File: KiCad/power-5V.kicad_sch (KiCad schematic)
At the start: 0 parts

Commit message: chore(pcb): split voltage regulators to separate schematics
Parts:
- added U?: TPS84320RUQR, RUQ_47, symbol Buck converter:TPS84320RUQR
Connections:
- new net 5V: U?.21 (VO), U?.24 (VO), U?.25 (VO), U?.26 (VO), U?.27 (VO), U?.28 (VO), U?.29 (VO), U?.47 (VO)
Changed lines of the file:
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@@
 (kicad_sch (version 20211123) (generator eeschema)
   (paper "A4")
+  (junction (at 178.6128 78.3336) (diameter 0) (color 0 0 0 0)
+  )
+  (junction (at 178.6128 80.8736) (diameter 0) (color 0 0 0 0)
+  )
+  (junction (at 178.6128 75.7936) (diameter 0) (color 0 0 0 0)
+  )
+  (junction (at 178.6128 73.2536) (diameter 0) (color 0 0 0 0)
+  )
+  (junction (at 178.6128 68.1736) (diameter 0) (color 0 0 0 0)
+  )
+  (junction (at 178.6128 70.7136) (diameter 0) (color 0 0 0 0)
+  )
+  (junction (at 178.6128 65.6336) (diameter 0) (color 0 0 0 0)
+  )
+  (wire (pts (xy 178.6128 80.8736) (xy 178.6128 83.4136))
+    (stroke (width 0) (type default) (color 0 0 0 0))
+  )
+  (wire (pts (xy 178.6128 70.7136) (xy 178.6128 73.2536))
+    (stroke (width 0) (type default) (color 0 0 0 0))
+  )
+  (wire (pts (xy 178.6128 75.7936) (xy 178.6128 78.3336))
+    (stroke (width 0) (type default) (color 0 0 0 0))
+  )
+  (wire (pts (xy 178.6128 63.0936) (xy 181.1528 63.0936))
+    (stroke (width 0) (type default) (color 0 0 0 0))
+  )
+  (wire (pts (xy 178.6128 78.3336) (xy 178.6128 80.8736))
+    (stroke (width 0) (type default) (color 0 0 0 0))
+  )
+  (wire (pts (xy 178.6128 65.6336) (xy 178.6128 68.1736))
+    (stroke (width 0) (type default) (color 0 0 0 0))
+  )
+  (wire (pts (xy 178.6128 63.0936) (xy 178.6128 65.6336))
+    (stroke (width 0) (type default) (color 0 0 0 0))
+  )
+  (wire (pts (xy 178.6128 73.2536) (xy 178.6128 75.7936))
+    (stroke (width 0) (type default) (color 0 0 0 0))
+  )
+  (wire (pts (xy 178.6128 68.1736) (xy 178.6128 70.7136))
+    (stroke (width 0) (type default) (color 0 0 0 0))
+  )
+  (global_label "5V" (shape input) (at 181.1528 63.0936 0) (fields_autoplaced)
+    (effects (font (size 1.27 1.27)) (justify left))
+    (property "Intersheet References" "${INTERSHEET_REFS}" (id 0) (at 185.864 63.0142 0)
+      (effects (font (size 1.27 1.27)) (justify left) hide)
+    )
+  )
+  (symbol (lib_id "Buck converter:TPS84320RUQR") (at 127.8128 55.4736 0) (unit 1)
+    (in_bom yes) (on_board yes) (fields_autoplaced)
+    (property "Reference" "U?" (id 0) (at 153.2128 44.0436 0)
+      (effects (font (size 1.524 1.524)))
+    )
+    (property "Value" "TPS84320RUQR" (id 1) (at 153.2128 47.8536 0)
+      (effects (font (size 1.524 1.524)))
+    )
+    (property "Footprint" "RUQ_47" (id 2) (at 153.2128 49.3776 0)
+      (effects (font (size 1.524 1.524)) hide)
+    )
+    (property "Datasheet" "" (id 3) (at 127.8128 55.4736 0)
+      (effects (font (size 1.524 1.524)))
+    )
+    (pin "1")
+    (pin "10")
+    (pin "11")
+    (pin "12")
+    (pin "13")
+    (pin "14")
+    (pin "15")
+    (pin "16")
+    (pin "17")
+    (pin "18")
+    (pin "19")
+    (pin "2")
+    (pin "20")
+    (pin "21")
+    (pin "22")
+    (pin "23")
+    (pin "24")
+    (pin "25")
+    (pin "26")
+    (pin "27")
+    (pin "28")
+    (pin "29")
+    (pin "3")
+    (pin "30")
+    (pin "31")
+    (pin "32")
+    (pin "33")
+    (pin "34")
+    (pin "35")
+    (pin "36")
+    (pin "37")
+    (pin "38")
+    (pin "39")
+    (pin "4")
+    (pin "40")
+    (pin "41")
+    (pin "42")
+    (pin "43")
+    (pin "44")
+    (pin "45")
+    (pin "46")
+    (pin "47")
+    (pin "5")
+    (pin "6")
+    (pin "7")
+    (pin "8")
+    (pin "9")
+  )
 )

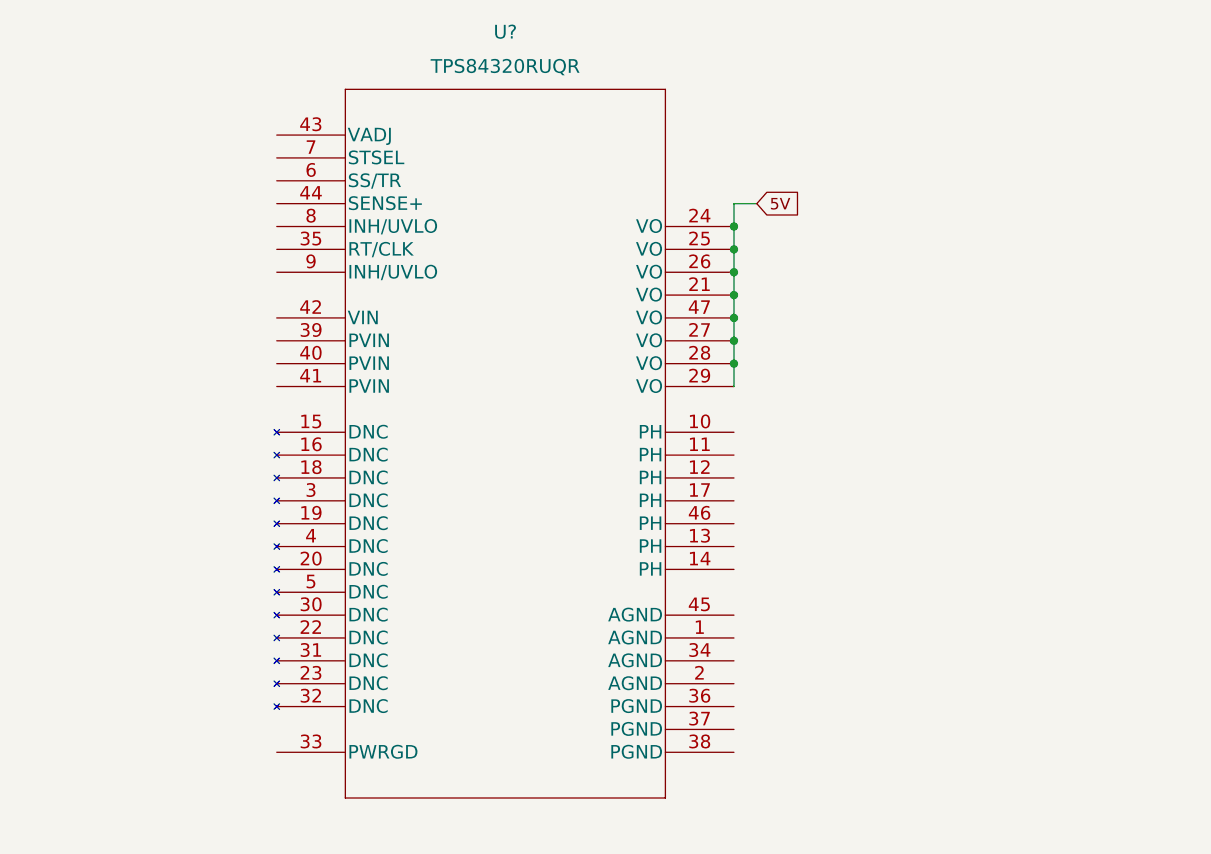
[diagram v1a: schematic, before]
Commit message: chore(pcb): start from scratch using TPSM63606RDLR
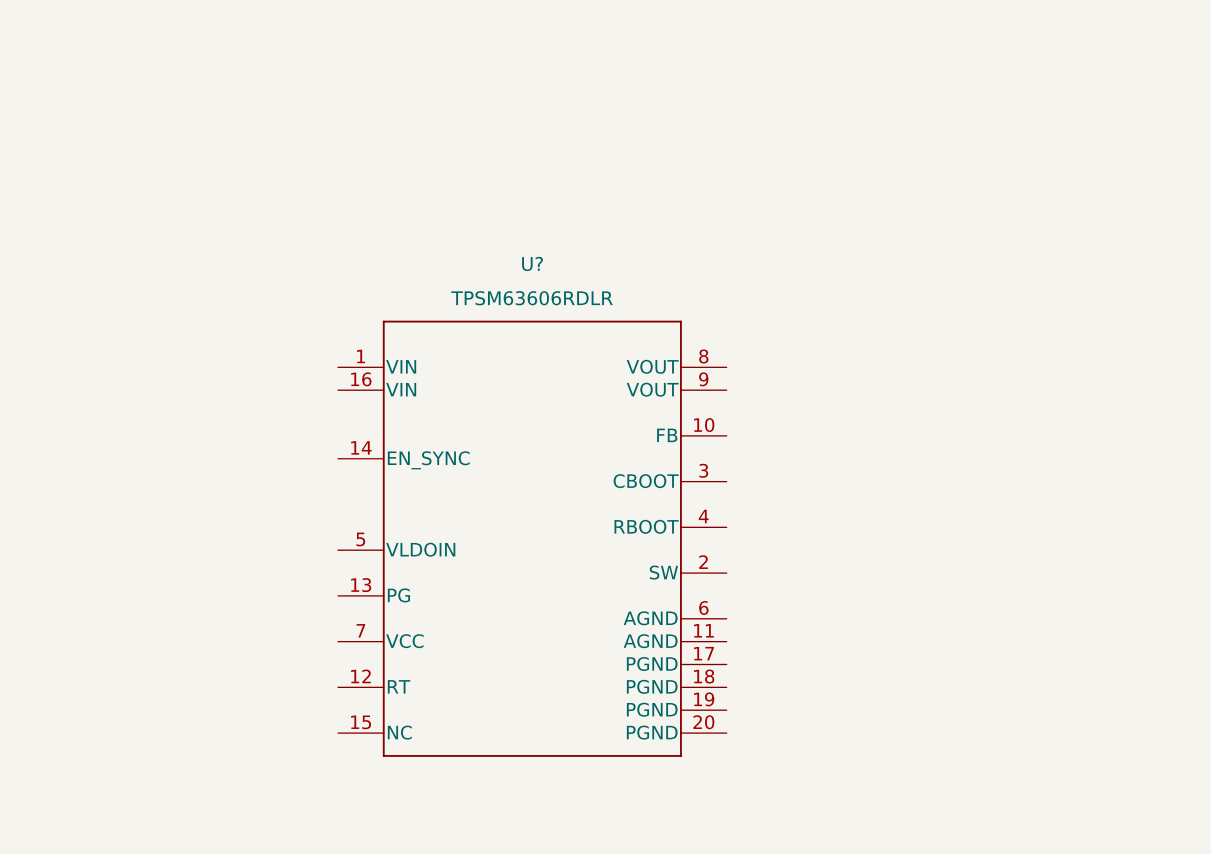
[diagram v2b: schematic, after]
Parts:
- removed U?: TPS84320RUQR, RUQ_47, symbol Buck converter:TPS84320RUQR
- added U?: TPSM63606RDLR, RDL0020A-MFG, symbol Power module:TPSM63606RDLR
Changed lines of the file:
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@@
 (kicad_sch (version 20211123) (generator eeschema)
   (paper "A4")
-  (junction (at 178.6128 78.3336) (diameter 0) (color 0 0 0 0)
-  )
-  (junction (at 178.6128 80.8736) (diameter 0) (color 0 0 0 0)
-  )
-  (junction (at 178.6128 75.7936) (diameter 0) (color 0 0 0 0)
-  )
-  (junction (at 178.6128 73.2536) (diameter 0) (color 0 0 0 0)
-  )
-  (junction (at 178.6128 68.1736) (diameter 0) (color 0 0 0 0)
-  )
-  (junction (at 178.6128 70.7136) (diameter 0) (color 0 0 0 0)
-  )
-  (junction (at 178.6128 65.6336) (diameter 0) (color 0 0 0 0)
-  )
-  (wire (pts (xy 178.6128 80.8736) (xy 178.6128 83.4136))
-    (stroke (width 0) (type default) (color 0 0 0 0))
-  )
-  (wire (pts (xy 178.6128 70.7136) (xy 178.6128 73.2536))
-    (stroke (width 0) (type default) (color 0 0 0 0))
-  )
-  (wire (pts (xy 178.6128 75.7936) (xy 178.6128 78.3336))
-    (stroke (width 0) (type default) (color 0 0 0 0))
-  )
-  (wire (pts (xy 178.6128 63.0936) (xy 181.1528 63.0936))
-    (stroke (width 0) (type default) (color 0 0 0 0))
-  )
-  (wire (pts (xy 178.6128 78.3336) (xy 178.6128 80.8736))
-    (stroke (width 0) (type default) (color 0 0 0 0))
-  )
-  (wire (pts (xy 178.6128 65.6336) (xy 178.6128 68.1736))
-    (stroke (width 0) (type default) (color 0 0 0 0))
-  )
-  (wire (pts (xy 178.6128 63.0936) (xy 178.6128 65.6336))
-    (stroke (width 0) (type default) (color 0 0 0 0))
-  )
-  (wire (pts (xy 178.6128 73.2536) (xy 178.6128 75.7936))
-    (stroke (width 0) (type default) (color 0 0 0 0))
-  )
-  (wire (pts (xy 178.6128 68.1736) (xy 178.6128 70.7136))
-    (stroke (width 0) (type default) (color 0 0 0 0))
-  )
-  (global_label "5V" (shape input) (at 181.1528 63.0936 0) (fields_autoplaced)
-    (effects (font (size 1.27 1.27)) (justify left))
-    (property "Intersheet References" "${INTERSHEET_REFS}" (id 0) (at 185.864 63.0142 0)
-      (effects (font (size 1.27 1.27)) (justify left) hide)
-    )
-  )
-  (symbol (lib_id "Buck converter:TPS84320RUQR") (at 127.8128 55.4736 0) (unit 1)
+  (symbol (lib_id "Power module:TPSM63606RDLR") (at 134.62 81.28 0) (unit 1)
     (in_bom yes) (on_board yes) (fields_autoplaced)
-    (property "Reference" "U?" (id 0) (at 153.2128 44.0436 0)
+    (property "Reference" "U?" (id 0) (at 156.21 69.85 0)
       (effects (font (size 1.524 1.524)))
     )
-    (property "Value" "TPS84320RUQR" (id 1) (at 153.2128 47.8536 0)
+    (property "Value" "TPSM63606RDLR" (id 1) (at 156.21 73.66 0)
       (effects (font (size 1.524 1.524)))
     )
-    (property "Footprint" "RUQ_47" (id 2) (at 153.2128 49.3776 0)
+    (property "Footprint" "RDL0020A-MFG" (id 2) (at 134.62 82.804 0)
       (effects (font (size 1.524 1.524)) hide)
     )
-    (property "Datasheet" "" (id 3) (at 127.8128 55.4736 0)
+    (property "Datasheet" "" (id 3) (at 134.62 81.28 0)
       (effects (font (size 1.524 1.524)))
     )
@@
     (pin "2")
     (pin "20")
-    (pin "21")
-    (pin "22")
-    (pin "23")
-    (pin "24")
-    (pin "25")
-    (pin "26")
-    (pin "27")
-    (pin "28")
-    (pin "29")
     (pin "3")
-    (pin "30")
-    (pin "31")
-    (pin "32")
-    (pin "33")
-    (pin "34")
-    (pin "35")
-    (pin "36")
-    (pin "37")
-    (pin "38")
-    (pin "39")
     (pin "4")
-    (pin "40")
-    (pin "41")
-    (pin "42")
-    (pin "43")
-    (pin "44")
-    (pin "45")
-    (pin "46")
-    (pin "47")
     (pin "5")
     (pin "6")

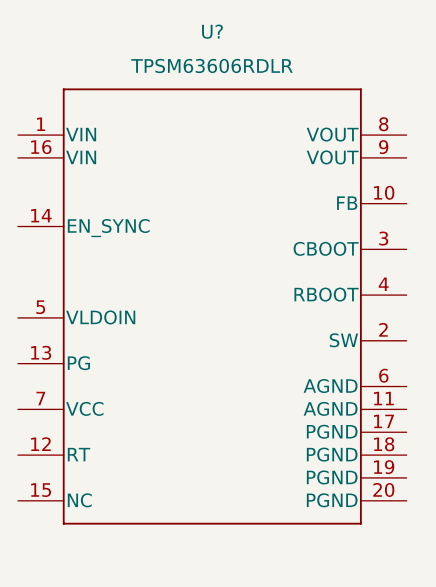
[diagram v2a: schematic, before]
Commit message: feat(pcb): add schematic for battery
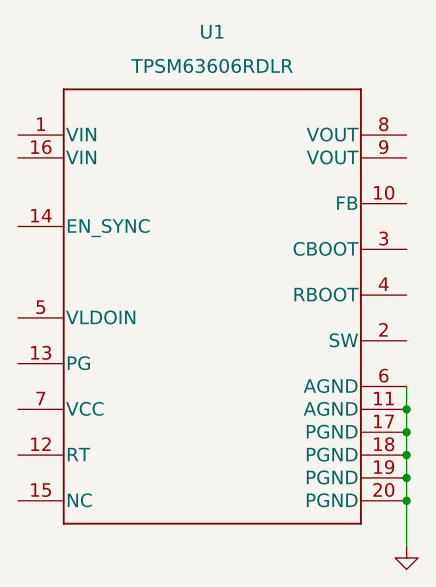
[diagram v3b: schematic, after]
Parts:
- gave numbers to parts that had none: 1
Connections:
- net GND: now reaches U1.11 (AGND)
- net GND: now also U1.17 (PGND), U1.18 (PGND), U1.19 (PGND), U1.20 (PGND), U1.6 (AGND)
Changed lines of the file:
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@@
 (kicad_sch (version 20211123) (generator eeschema)
   (paper "A4")
+  (junction (at 177.8 116.84) (diameter 0) (color 0 0 0 0)
+  )
+  (junction (at 177.8 121.92) (diameter 0) (color 0 0 0 0)
+  )
+  (junction (at 177.8 119.38) (diameter 0) (color 0 0 0 0)
+  )
+  (junction (at 177.8 114.3) (diameter 0) (color 0 0 0 0)
+  )
+  (junction (at 177.8 111.76) (diameter 0) (color 0 0 0 0)
+  )
+  (wire (pts (xy 177.8 114.3) (xy 177.8 116.84))
+    (stroke (width 0) (type default) (color 0 0 0 0))
+  )
+  (wire (pts (xy 177.8 109.22) (xy 177.8 111.76))
+    (stroke (width 0) (type default) (color 0 0 0 0))
+  )
+  (wire (pts (xy 177.8 121.92) (xy 177.8 127))
+    (stroke (width 0) (type default) (color 0 0 0 0))
+  )
+  (wire (pts (xy 177.8 119.38) (xy 177.8 121.92))
+    (stroke (width 0) (type default) (color 0 0 0 0))
+  )
+  (wire (pts (xy 177.8 116.84) (xy 177.8 119.38))
+    (stroke (width 0) (type default) (color 0 0 0 0))
+  )
+  (wire (pts (xy 177.8 111.76) (xy 177.8 114.3))
+    (stroke (width 0) (type default) (color 0 0 0 0))
+  )
+  (symbol (lib_id "power:GND") (at 177.8 127 0) (unit 1)
+    (in_bom yes) (on_board yes) (fields_autoplaced)
+    (property "Reference" "#PWR0103" (id 0) (at 177.8 133.35 0)
+      (effects (font (size 1.27 1.27)) hide)
+    )
+    (property "Value" "" (id 1) (at 177.8 132.08 0))
+    (property "Footprint" "" (id 2) (at 177.8 127 0)
+      (effects (font (size 1.27 1.27)) hide)
+    )
+    (property "Datasheet" "" (id 3) (at 177.8 127 0)
+      (effects (font (size 1.27 1.27)) hide)
+    )
+    (pin "1")
+  )
   (symbol (lib_id "Power module:TPSM63606RDLR") (at 134.62 81.28 0) (unit 1)
     (in_bom yes) (on_board yes) (fields_autoplaced)
-    (property "Reference" "U?" (id 0) (at 156.21 69.85 0)
+    (property "Reference" "U1" (id 0) (at 156.21 69.85 0)
       (effects (font (size 1.524 1.524)))
     )

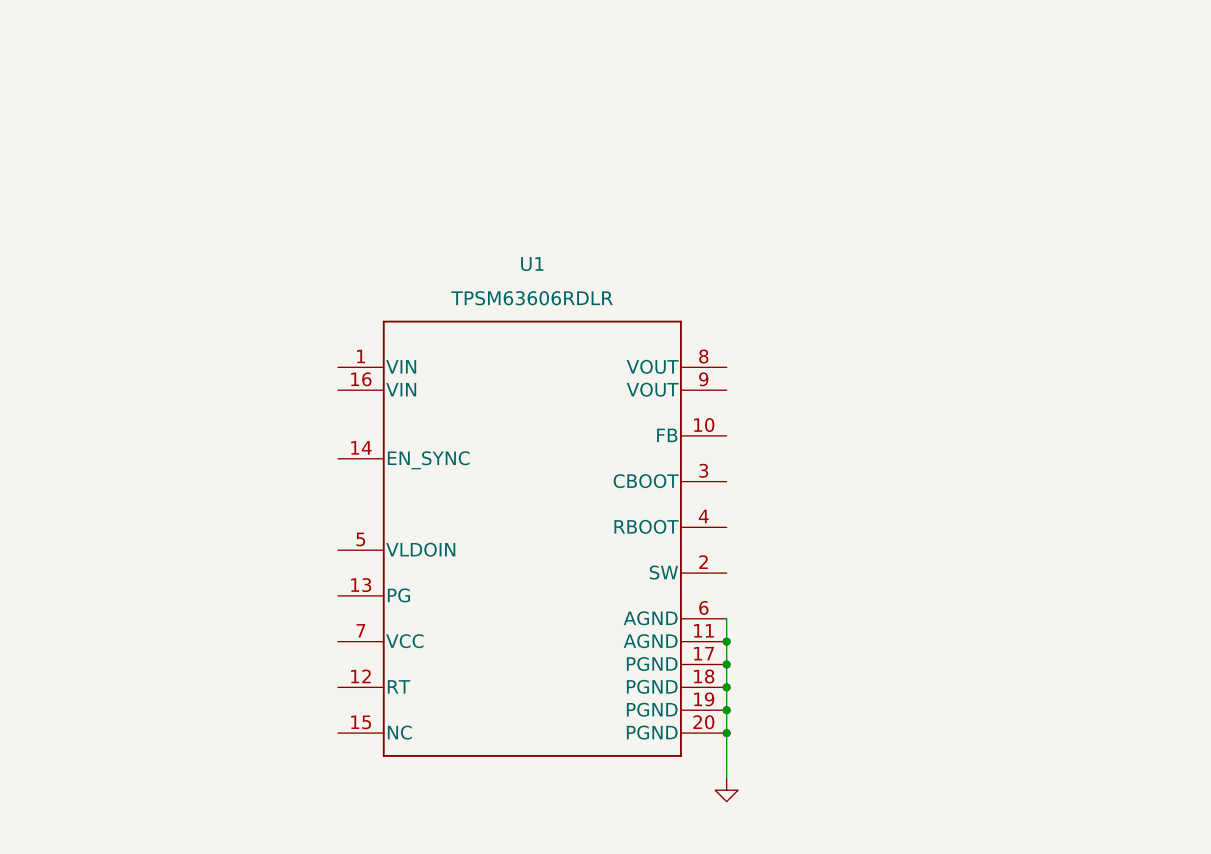
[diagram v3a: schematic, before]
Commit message: feat(pcb): add input capacitors
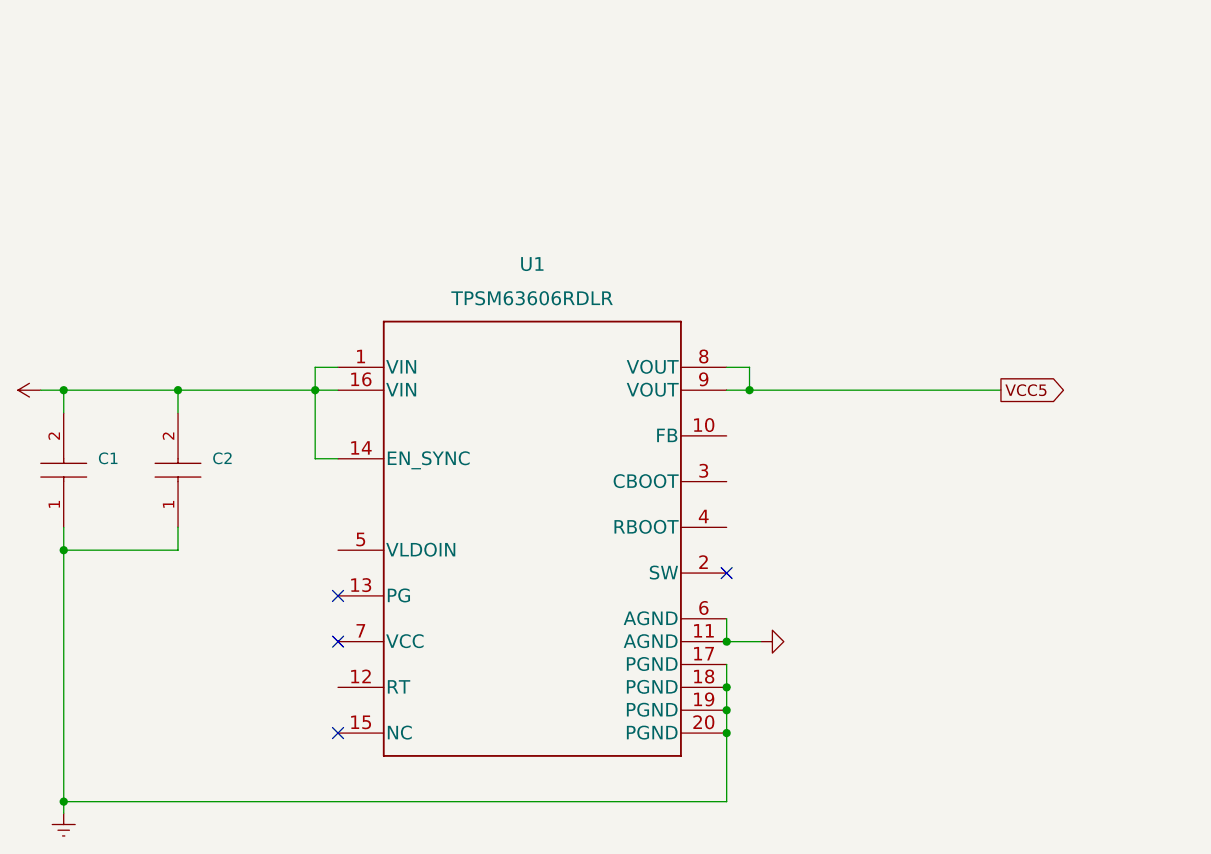
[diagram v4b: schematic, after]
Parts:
- added C1, C2: (no value), symbol C3225X7R1H106M250AC:C3225X7R1H106M250AC
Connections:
- net GND: no longer U1.17 (PGND), U1.18 (PGND), U1.19 (PGND), U1.20 (PGND)
- net +BATT: now reaches U1.1 (VIN)
- net +BATT: now also U1.14 (EN_SYNC), U1.16 (VIN), C1.2, C2.2
- net VCC5: now reaches U1.8 (VOUT)
- net VCC5: now also U1.9 (VOUT)
- new net GNDREF: C1.1, C2.1, U1.17 (PGND), U1.18 (PGND), U1.19 (PGND), U1.20 (PGND)
- no-connect marks 0 -> 4
